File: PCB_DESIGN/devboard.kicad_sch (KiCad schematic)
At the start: 0 parts

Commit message: working on power stuff
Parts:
- added U1: RP2040, Package_DFN_QFN:QFN-56-1EP_7x7mm_P0.4mm_EP3.2x3.2mm, symbol MCU_RaspberryPi:RP2040
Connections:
- new net +1V1: U1.23 (DVDD), U1.45 (VREG_VOUT), U1.50 (DVDD)
- new net +3V3: U1.1 (IOVDD), U1.10 (IOVDD), U1.22 (IOVDD), U1.33 (IOVDD), U1.42 (IOVDD), U1.43 (ADC_AVDD), U1.44 (VREG_IN), U1.48 (USB_VDD), U1.49 (IOVDD)

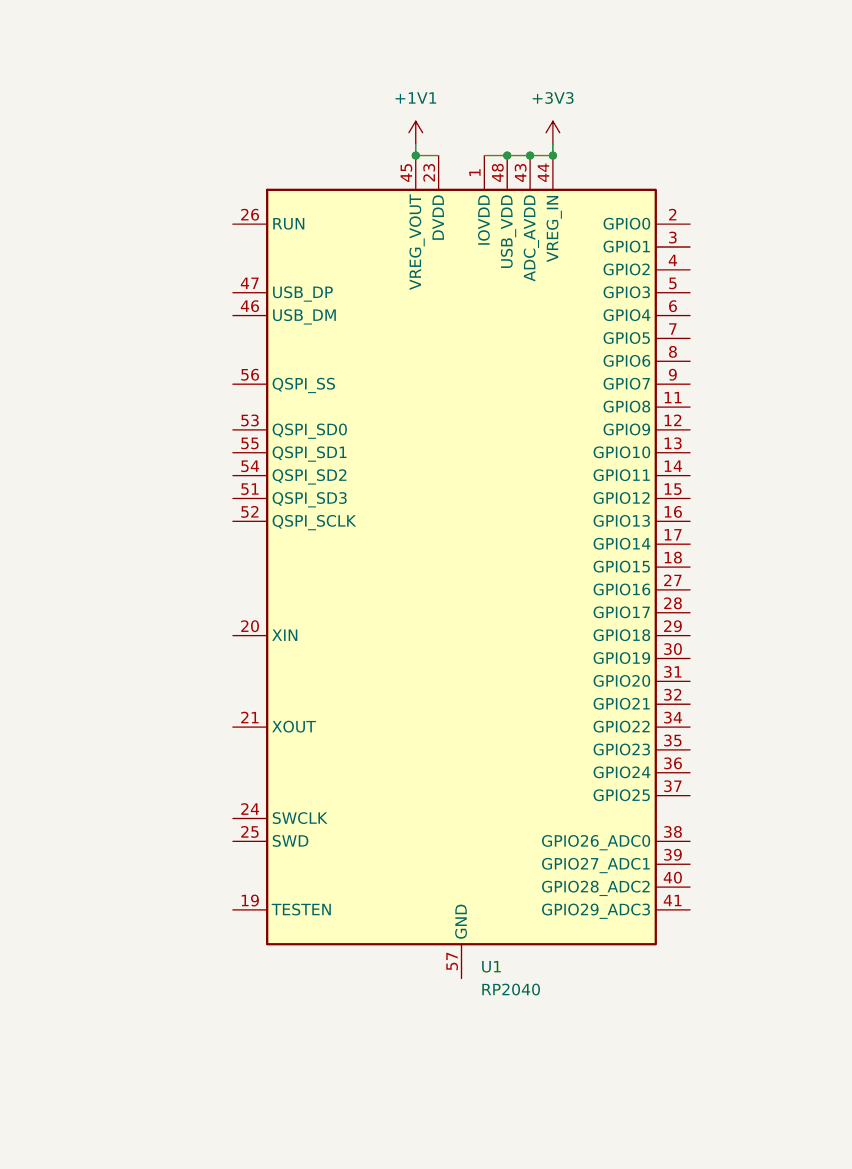
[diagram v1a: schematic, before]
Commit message: finished power decoupling
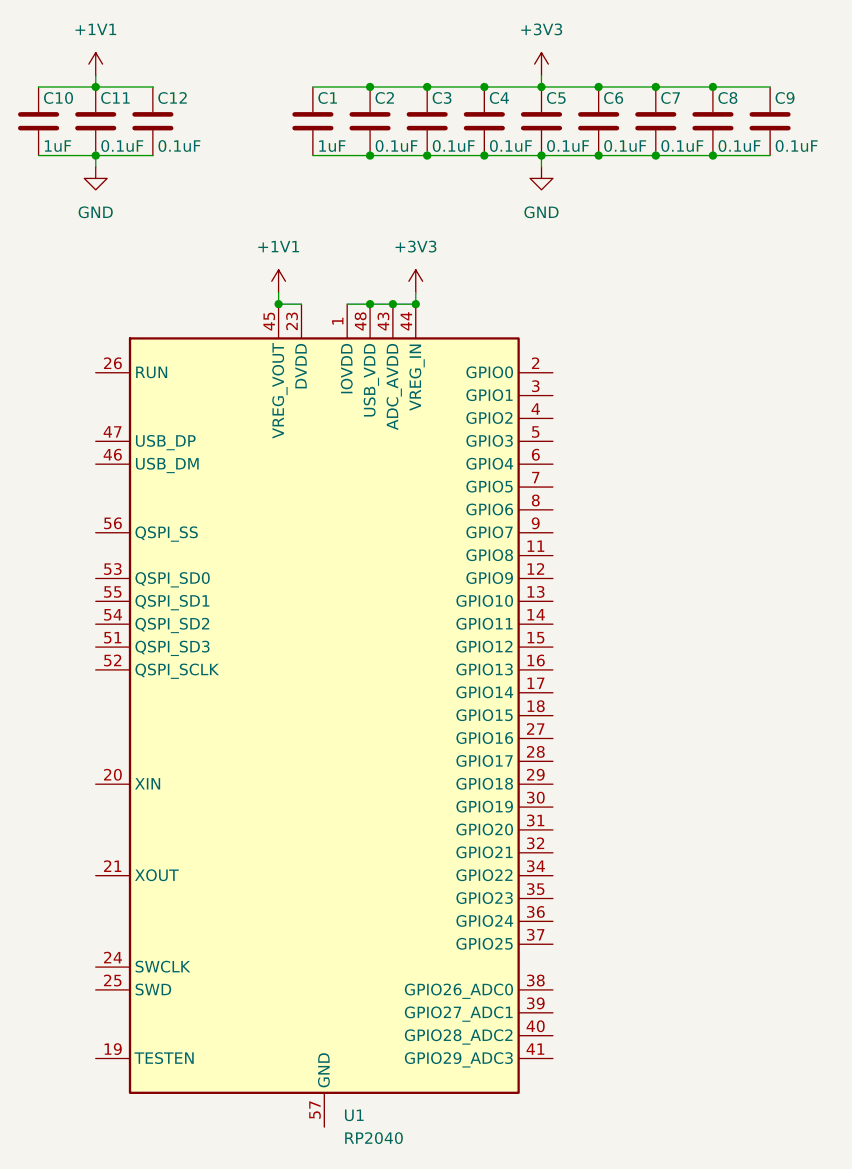
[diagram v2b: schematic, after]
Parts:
- added C1, C10: 1uF, symbol Device:C
- added C11, C12, C2, C3, C4, C5, C6, C7, C8, C9: 0.1uF, symbol Device:C
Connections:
- net +1V1: now also C10.1, C11.1, C12.1
- net +3V3: now also C1.1, C2.1, C3.1, C4.1, C5.1, C6.1, C7.1, C8.1, C9.1
- new net GND: C1.2, C10.2, C11.2, C12.2, C2.2, C3.2, C4.2, C5.2, C6.2, C7.2, C8.2, C9.2
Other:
- moved on the sheet: U1

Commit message: working on USB
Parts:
- added J1: USB_C_Receptacle_USB2.0_14P, symbol Connector:USB_C_Receptacle_USB2.0_14P
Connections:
- net GND: now also U1.57 (GND), J1.A1 (GND), J1.A12 (GND), J1.B1 (GND), J1.B12 (GND), J1.S1 (SHIELD)
- new net: J1.A4 (VBUS), J1.A9 (VBUS), J1.B4 (VBUS), J1.B9 (VBUS)
- new net USB_D+: J1.A6 (D+), J1.A7 (D-), J1.B6 (D+), J1.B7 (D-)

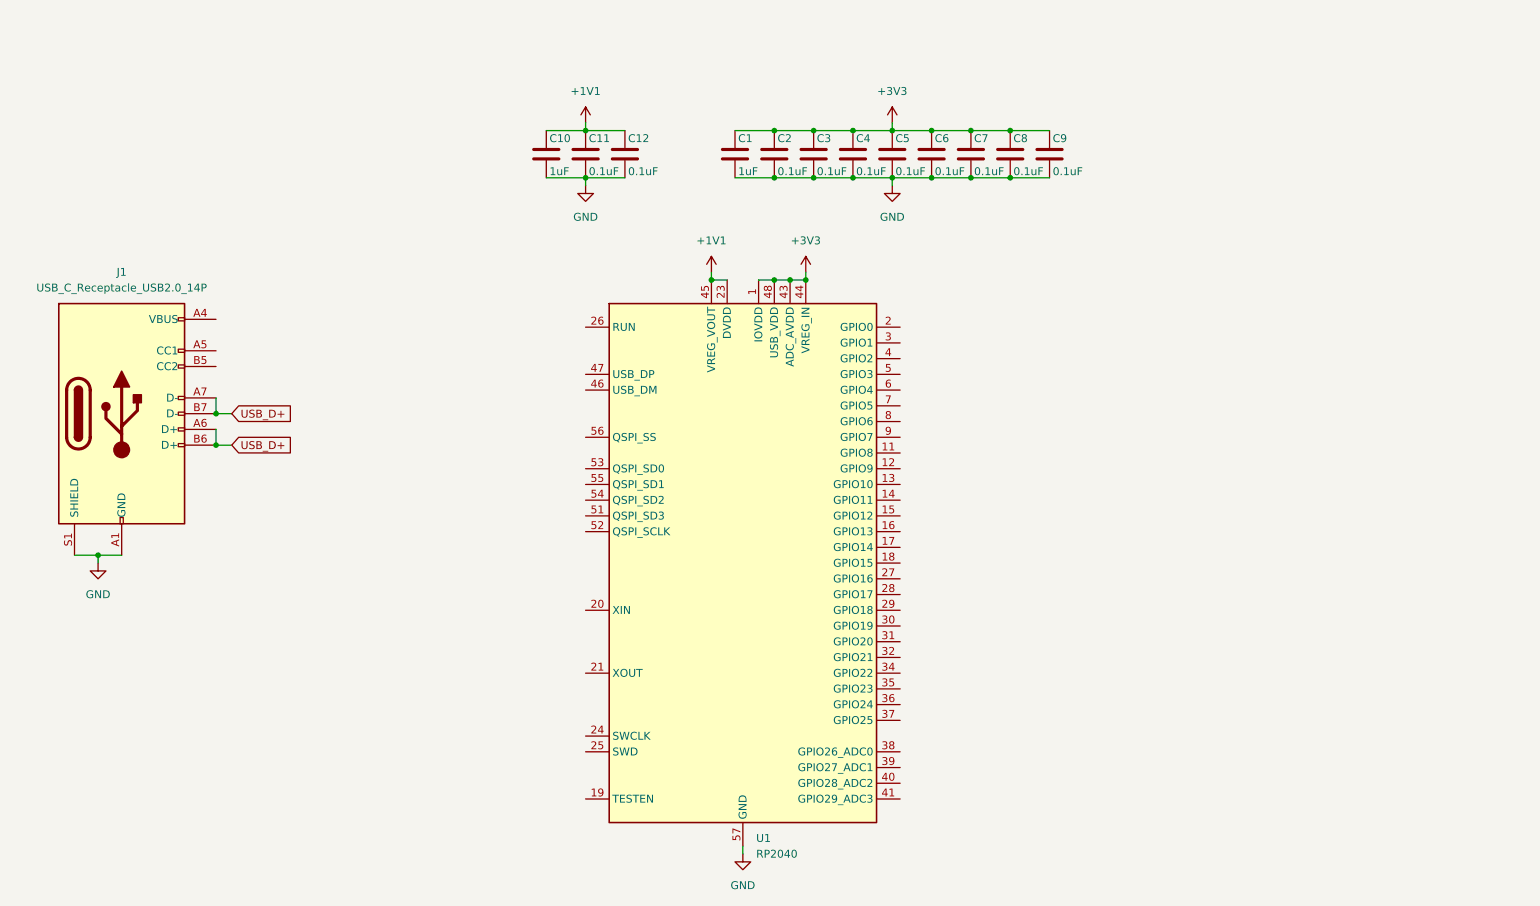
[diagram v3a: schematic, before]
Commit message: finished USB-C wiring
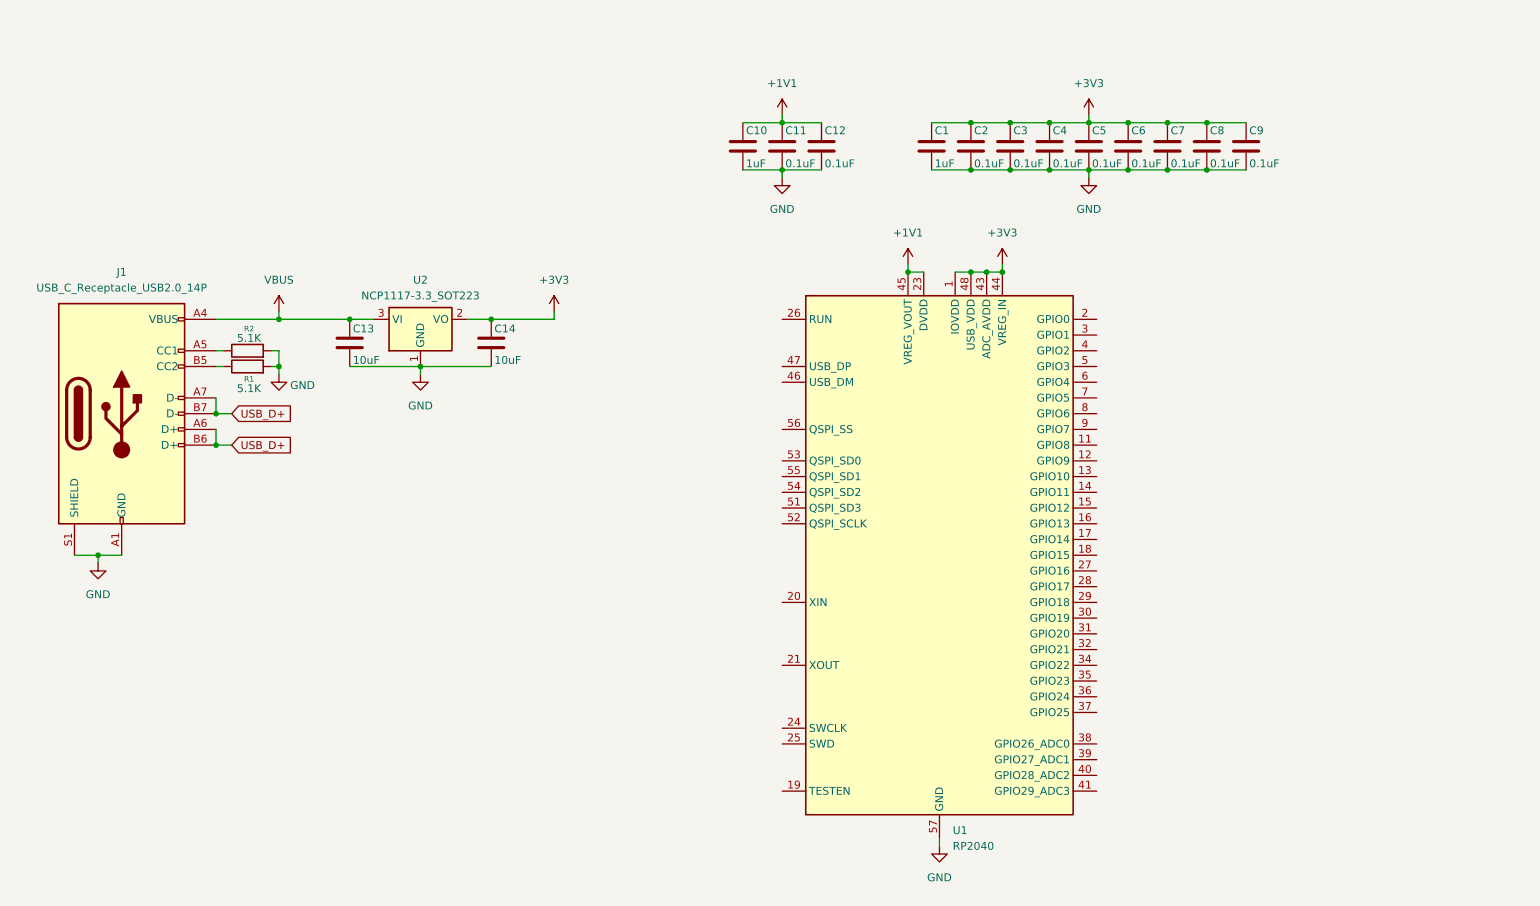
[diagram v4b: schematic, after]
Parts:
- added C13, C14: 10uF, symbol Device:C
- added R1, R2: 5.1K, symbol Device:R
- added U2: NCP1117-3.3_SOT223, Package_TO_SOT_SMD:SOT-223-3_TabPin2, symbol Regulator_Linear:NCP1117-3.3_SOT223
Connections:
- net +3V3: now also C14.1, U2.2 (VO)
- net GND: now also C13.2, C14.2, R1.2, R2.2, U2.1 (GND)
- net VBUS: now reaches J1.A4 (VBUS), J1.A9 (VBUS), J1.B4 (VBUS), J1.B9 (VBUS)
- net VBUS: now also C13.1, U2.3 (VI)
- net at J1.A5 (CC1): now also R2.1
- net at J1.B5 (CC2): now also R1.1
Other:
- moved on the sheet: C1, C10, C11, C12, C2, C3, C4, C5, C6, C7, C8, C9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

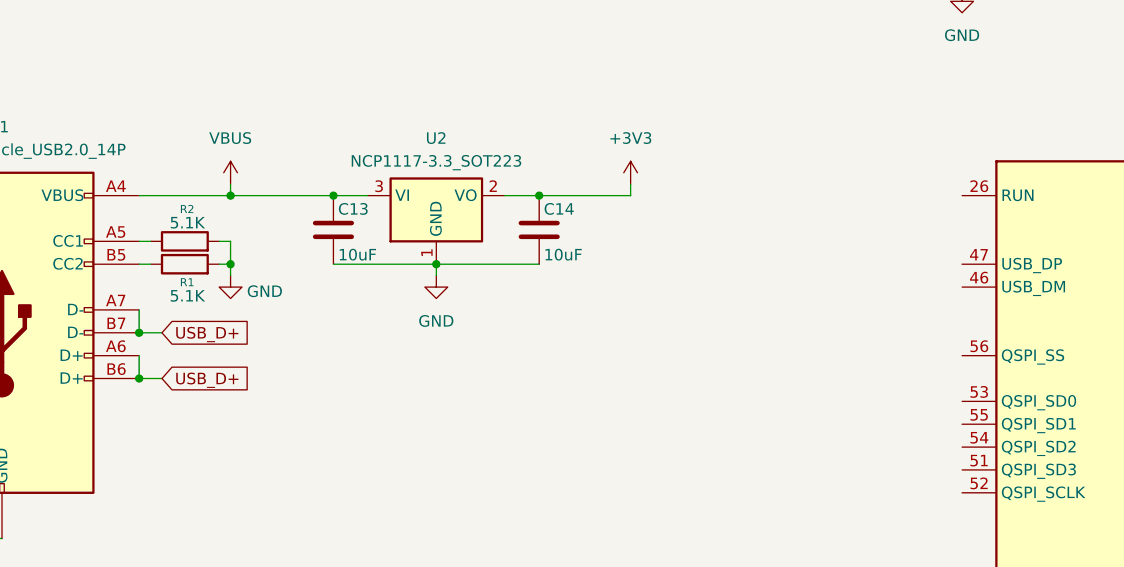
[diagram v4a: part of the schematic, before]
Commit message: fixing the journal and USB on MCU
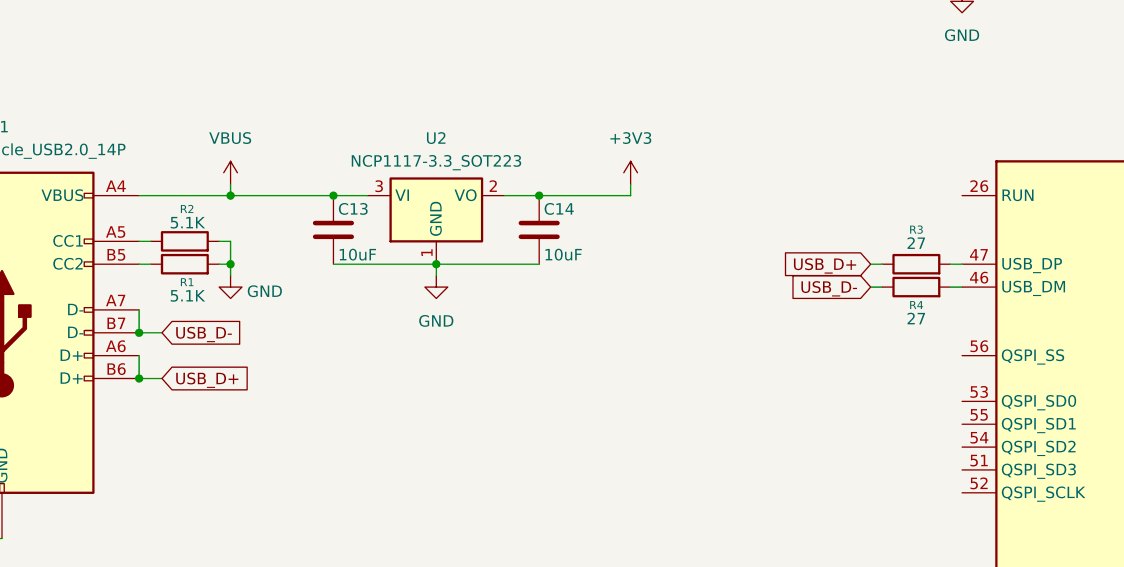
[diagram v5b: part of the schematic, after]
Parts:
- added R3, R4: 27, symbol Device:R
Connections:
- net USB_D+: now also R3.1; no longer J1.A7 (D-), J1.B7 (D-)
- net at U1.46 (USB_DM): now also R4.2
- net at U1.47 (USB_DP): now also R3.2
- new net USB_D-: J1.A7 (D-), J1.B7 (D-), R4.1
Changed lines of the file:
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@@
+	(wire
+		(pts
+			(xy 135.89 82.55) (xy 137.16 82.55)
+		)
+		(stroke
+			(width 0)
+			(type default)
+		)
+	)
 	(wire
 		(pts
@@
 	(wire
 		(pts
+			(xy 144.78 80.01) (xy 146.05 80.01)
+		)
+		(stroke
+			(width 0)
+			(type default)
+		)
+	)
+	(wire
+		(pts
+			(xy 144.78 82.55) (xy 146.05 82.55)
+		)
+		(stroke
+			(width 0)
+			(type default)
+		)
+	)
+	(wire
+		(pts
+			(xy 135.89 80.01) (xy 137.16 80.01)
+		)
+		(stroke
+			(width 0)
+			(type default)
+		)
+	)
+	(wire
+		(pts
 			(xy 166.37 63.5) (xy 166.37 64.77)
 		)
@@
 		)
 	)
+	(global_label "USB_D-"
+		(shape input)
+		(at 135.89 82.55 180)
+		(fields_autoplaced yes)
+		(effects
+			(font
+				(size 1.27 1.27)
+			)
+			(justify right)
+		)
+		(property "Intersheetrefs" "${INTERSHEET_REFS}"
+			(at 125.2848 82.55 0)
+			(effects
+				(font
+					(size 1.27 1.27)
+				)
+				(justify right)
+				(hide yes)
+			)
+		)
+	)
 	(global_label "USB_D+"
+		(shape input)
+		(at 135.89 80.01 180)
+		(fields_autoplaced yes)
+		(effects
+			(font
+				(size 1.27 1.27)
+			)
+			(justify right)
+		)
+		(property "Intersheetrefs" "${INTERSHEET_REFS}"
+			(at 125.2848 80.01 0)
+			(effects
+				(font
+					(size 1.27 1.27)
+				)
+				(justify right)
+				(hide yes)
+			)
+		)
+	)
+	(global_label "USB_D-"
 		(shape input)
 		(at 57.15 87.63 0)
@@
 	)
 	(symbol
+		(lib_id "Device:R")
+		(at 140.97 80.01 90)
+		(unit 1)
+		(exclude_from_sim no)
+		(in_bom yes)
+		(on_board yes)
+		(dnp no)
+		(property "Reference" "R3"
+			(at 140.97 76.2 90)
+			(effects
+				(font
+					(size 0.889 0.889)
+				)
+			)
+		)
+		(property "Value" "27"
+			(at 140.97 77.724 90)
+			(effects
+				(font
+					(size 1.27 1.27)
+				)
+			)
+		)
+		(property "Footprint" ""
+			(at 140.97 81.788 90)
+			(effects
+				(font
+					(size 1.27 1.27)
+				)
+				(hide yes)
+			)
+		)
+		(property "Datasheet" "~"
+			(at 140.97 80.01 0)
+			(effects
+				(font
+					(size 1.27 1.27)
+				)
+				(hide yes)
+			)
+		)
+		(property "Description" "Resistor"
+			(at 140.97 80.01 0)
+			(effects
+				(font
+					(size 1.27 1.27)
+				)
+				(hide yes)
+			)
+		)
+		(pin "2"
+		)
+		(pin "1"
+		)
+		(instances
+			(project ""
+				(path "/8a2a4d17-ab41-4dea-99ab-88cd6502c408"
+					(reference "R3")
+					(unit 1)
+				)
+			)
+		)
+	)
+	(symbol
 		(lib_id "Device:C")
 		(at 214.63 44.45 0)
@@
 					(unit 1)
 				)
+			)
+		)
+	)
+	(symbol
+		(lib_id "Device:R")
+		(at 140.97 82.55 90)
+		(unit 1)
+		(exclude_from_sim no)
+		(in_bom yes)
+		(on_board yes)
+		(dnp no)
+		(property "Reference" "R4"
+			(at 140.97 84.582 90)
+			(effects
+				(font
+					(size 0.889 0.889)
+				)
+			)
+		)
+		(property "Value" "27"
+			(at 140.97 86.106 90)
+			(effects
+				(font
+					(size 1.27 1.27)
+				)
+			)
+		)
+		(property "Footprint" ""
+			(at 140.97 84.328 90)
+			(effects
+				(font
+					(size 1.27 1.27)
+				)
+				(hide yes)
+			)
+		)
+		(property "Datasheet" "~"
+			(at 140.97 82.55 0)
+			(effects
+				(font
+					(size 1.27 1.27)
+				)
+				(hide yes)
+			)
+		)
+		(property "Description" "Resistor"
+			(at 140.97 82.55 0)
+			(effects
+				(font
+					(size 1.27 1.27)
+				)
+				(hide yes)
+			)
+		)
+		(pin "2"
+		)
+		(pin "1"
+		)
+		(instances
+			(project "devboard"
+				(path "/8a2a4d17-ab41-4dea-99ab-88cd6502c408"
+					(reference "R4")
+					(unit 1)
+				)
